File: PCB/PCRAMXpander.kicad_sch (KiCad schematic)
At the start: 24 parts, among them J1 Bus_ISA_16bit, U1 ATF16V8B-15PU, U2 SN74LVCR16245ADGGR, U3 SN74LVC16244ADGGR, U4 SN74LVC16244A, U5 AS6C3216A-55TIN, U6 AS6C3216A-55TIN, U7 SN74LVC573APWR

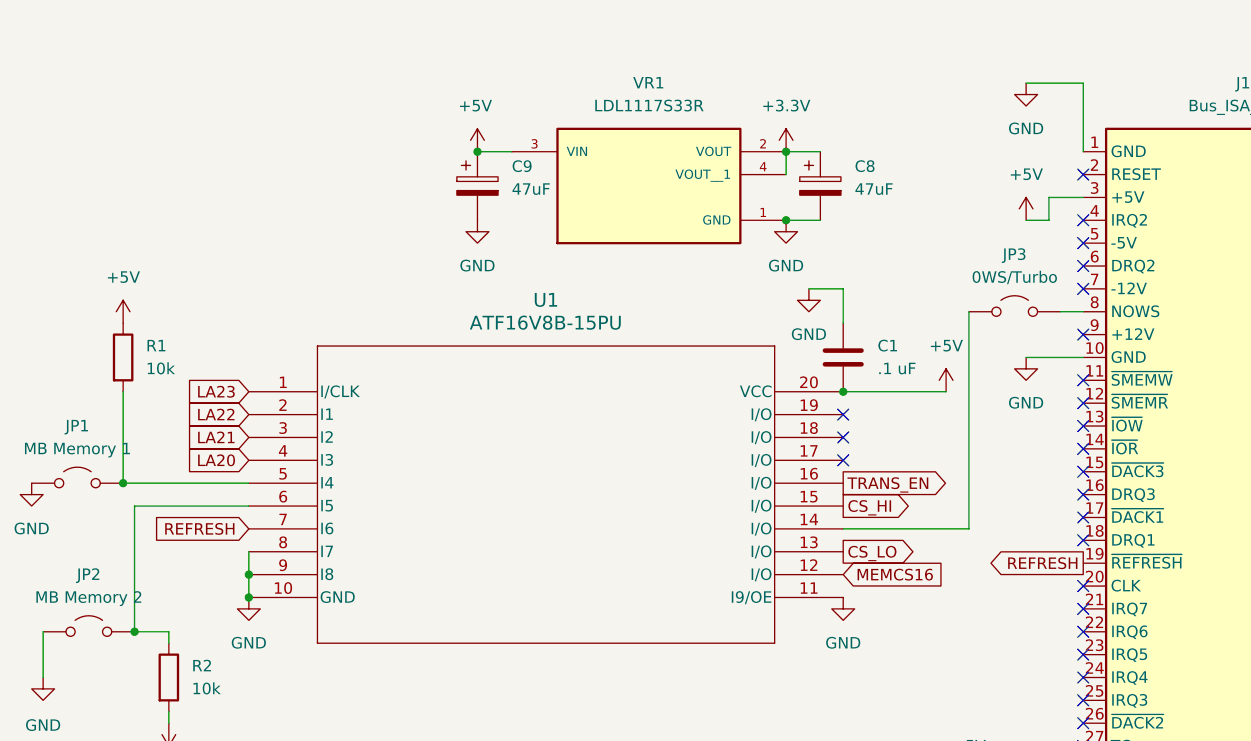
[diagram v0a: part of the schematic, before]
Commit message: Silkscreen updates, reset line wired
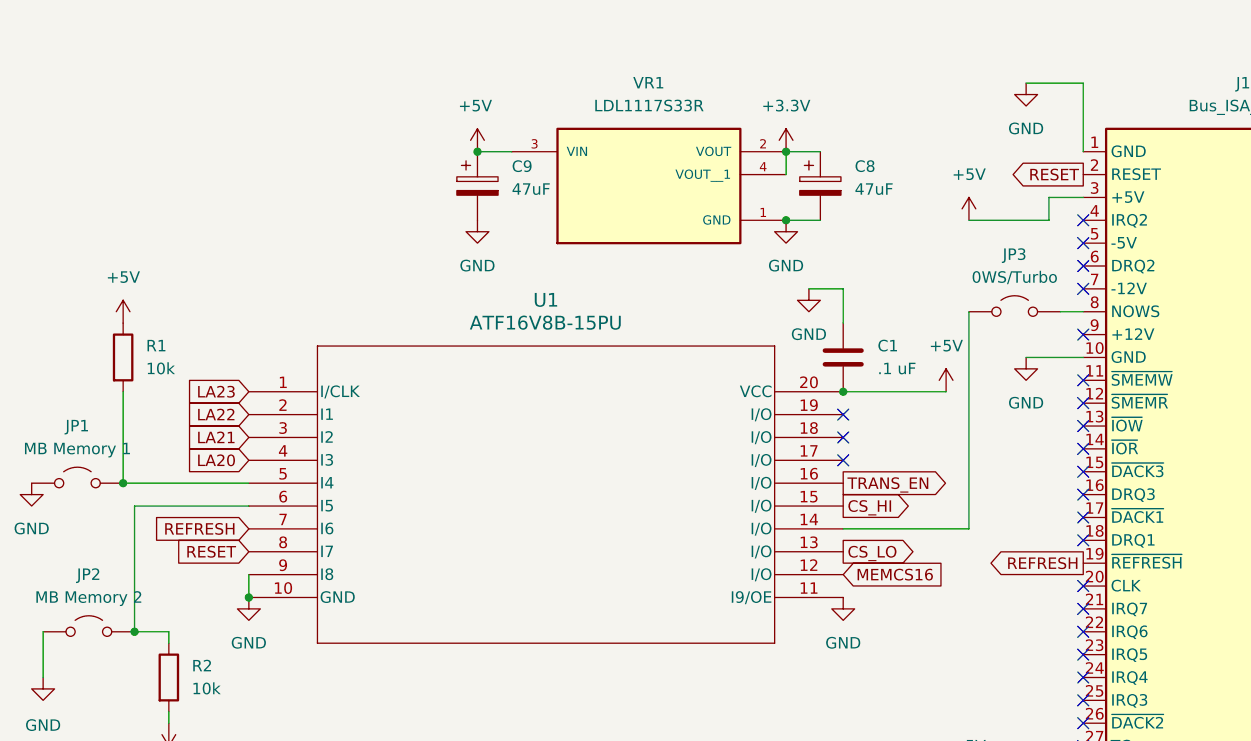
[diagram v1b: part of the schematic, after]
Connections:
- net GND: no longer U1.8 (I7)
- net RESET: now reaches J1.2 (RESET)
- net RESET: now also U1.8 (I7)
- no-connect marks 51 -> 50
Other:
- title: PC RAM Expander 8MB -> PCRAMXpander 8MB
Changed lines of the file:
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@@
 	(paper "B")
 	(title_block
-		(title "PC RAM Expander 8MB")
+		(title "PCRAMXpander 8MB")
 		(date "1/11/2026")
 		(rev "1.0")
@@
 	)
 	(junction
-		(at 41.91 179.07)
-		(diameter 0)
-		(color 0 0 0 0)
-	)
-	(junction
 		(at 278.13 43.18)
 		(diameter 0)
@@
 	)
 	(no_connect
-		(at 134.62 134.62)
-	)
-	(no_connect
 		(at 134.62 142.24)
 	)
@@
 	(wire
 		(pts
-			(xy 128.27 139.7) (xy 130.81 139.7)
+			(xy 121.92 139.7) (xy 130.81 139.7)
 		)
 		(stroke
@@
 	(wire
 		(pts
-			(xy 41.91 176.53) (xy 41.91 179.07)
-		)
-		(stroke
-			(width 0)
-			(type default)
-		)
-	)
-	(wire
-		(pts
 			(xy 195.58 194.31) (xy 212.09 194.31)
 		)
@@
 		)
 	)
+	(global_label "RESET"
+		(shape input)
+		(at 41.91 176.53 180)
+		(fields_autoplaced yes)
+		(effects
+			(font
+				(size 1.27 1.27)
+			)
+			(justify right)
+		)
+		(property "Intersheetrefs" "${INTERSHEET_REFS}"
+			(at 33.1797 176.53 0)
+			(effects
+				(font
+					(size 1.27 1.27)
+				)
+				(justify right)
+				(hide yes)
+			)
+		)
+	)
 	(global_label "D6"
 		(shape bidirectional)
@@
 		)
 	)
+	(global_label "RESET"
+		(shape output)
+		(at 134.62 134.62 180)
+		(fields_autoplaced yes)
+		(effects
+			(font
+				(size 1.27 1.27)
+			)
+			(justify right)
+		)
+		(property "Intersheetrefs" "${INTERSHEET_REFS}"
+			(at 125.8897 134.62 0)
+			(effects
+				(font
+					(size 1.27 1.27)
+				)
+				(justify right)
+				(hide yes)
+			)
+		)
+	)
 	(global_label "BA05"
 		(shape output)
@@
 	(symbol
 		(lib_id "power:+5V")
-		(at 128.27 139.7 0)
+		(at 121.92 139.7 0)
 		(unit 1)
 		(exclude_from_sim no)
@@
 		(fields_autoplaced yes)
 		(property "Reference" "#PWR024"
-			(at 128.27 143.51 0)
+			(at 121.92 143.51 0)
 			(effects
 				(font
@@
 		)
 		(property "Value" "+5V"
-			(at 128.27 134.62 0)
+			(at 121.92 134.62 0)
 			(effects
 				(font
@@
 		)
 		(property "Footprint" ""
-			(at 128.27 139.7 0)
+			(at 121.92 139.7 0)
 			(effects
 				(font
@@
 		)
 		(property "Datasheet" ""
-			(at 128.27 139.7 0)
+			(at 121.92 139.7 0)
 			(effects
 				(font
@@
 		)
 		(property "Description" "Power symbol creates a global label with name \"+5V\""
-			(at 128.27 139.7 0)
+			(at 121.92 139.7 0)
 			(effects
 				(font

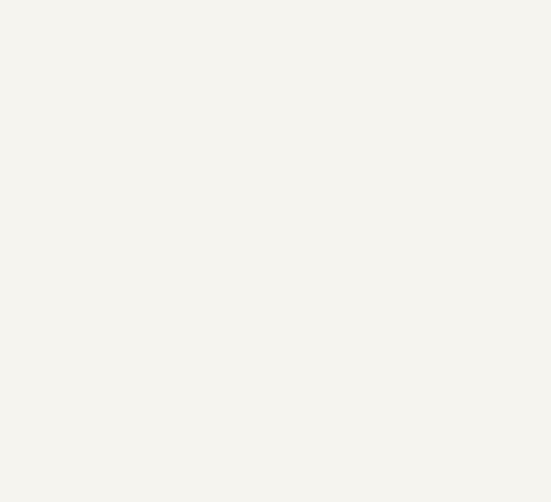
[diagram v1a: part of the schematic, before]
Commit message: Added mounting holes
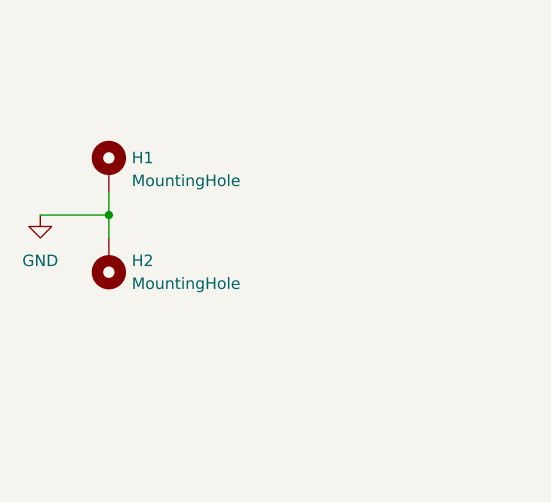
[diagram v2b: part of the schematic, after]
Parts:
- added H1, H2: MountingHole, MountingHole:MountingHole_3.2mm_M3_Pad_Via, symbol Mechanical:MountingHole_Pad
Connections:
- net GND: now also H1.1, H2.1
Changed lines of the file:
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@@
 	)
 	(junction
+		(at 25.4 36.83)
+		(diameter 0)
+		(color 0 0 0 0)
+	)
+	(junction
 		(at 321.31 81.28)
 		(diameter 0)
@@
 	(wire
 		(pts
+			(xy 25.4 34.29) (xy 25.4 36.83)
+		)
+		(stroke
+			(width 0)
+			(type default)
+		)
+	)
+	(wire
+		(pts
 			(xy 144.78 39.37) (xy 162.56 39.37)
 		)
@@
 	(wire
 		(pts
+			(xy 25.4 36.83) (xy 25.4 39.37)
+		)
+		(stroke
+			(width 0)
+			(type default)
+		)
+	)
+	(wire
+		(pts
 			(xy 313.69 199.39) (xy 323.85 199.39)
 		)
@@
 	(wire
 		(pts
+			(xy 17.78 36.83) (xy 25.4 36.83)
+		)
+		(stroke
+			(width 0)
+			(type default)
+		)
+	)
+	(wire
+		(pts
 			(xy 198.12 199.39) (xy 212.09 199.39)
 		)
@@
 	)
 	(symbol
+		(lib_id "Mechanical:MountingHole_Pad")
+		(at 25.4 41.91 180)
+		(unit 1)
+		(exclude_from_sim no)
+		(in_bom no)
+		(on_board yes)
+		(dnp no)
+		(fields_autoplaced yes)
+		(property "Reference" "H2"
+			(at 27.94 41.9099 0)
+			(effects
+				(font
+					(size 1.27 1.27)
+				)
+				(justify right)
+			)
+		)
+		(property "Value" "MountingHole"
+			(at 27.94 44.4499 0)
+			(effects
+				(font
+					(size 1.27 1.27)
+				)
+				(justify right)
+			)
+		)
+		(property "Footprint" "MountingHole:MountingHole_3.2mm_M3_Pad_Via"
+			(at 25.4 41.91 0)
+			(effects
+				(font
+					(size 1.27 1.27)
+				)
+				(hide yes)
+			)
+		)
+		(property "Datasheet" "~"
+			(at 25.4 41.91 0)
+			(effects
+				(font
+					(size 1.27 1.27)
+				)
+				(hide yes)
+			)
+		)
+		(property "Description" "Mounting Hole with connection"
+			(at 25.4 41.91 0)
+			(effects
+				(font
+					(size 1.27 1.27)
+				)
+				(hide yes)
+			)
+		)
+		(pin "1"
+		)
+		(instances
+			(project "PCRAMXpander"
+				(path "/1cf6e2a4-b983-419d-81f7-8fbd15ee10a7"
+					(reference "H2")
+					(unit 1)
+				)
+			)
+		)
+	)
+	(symbol
 		(lib_id "ATF16V8B_15PU_2026-01-01_19-13-25:ATF16V8B-15PU")
 		(at 41.91 158.75 0)
@@
 	)
 	(symbol
+		(lib_id "Mechanical:MountingHole_Pad")
+		(at 25.4 31.75 0)
+		(unit 1)
+		(exclude_from_sim no)
+		(in_bom no)
+		(on_board yes)
+		(dnp no)
+		(property "Reference" "H1"
+			(at 27.94 30.4799 0)
+			(effects
+				(font
+					(size 1.27 1.27)
+				)
+				(justify left)
+			)
+		)
+		(property "Value" "MountingHole"
+			(at 27.94 33.0199 0)
+			(effects
+				(font
+					(size 1.27 1.27)
+				)
+				(justify left)
+			)
+		)
+		(property "Footprint" "MountingHole:MountingHole_3.2mm_M3_Pad_Via"
+			(at 25.4 31.75 0)
+			(effects
+				(font
+					(size 1.27 1.27)
+				)
+				(hide yes)
+			)
+		)
+		(property "Datasheet" "~"
+			(at 25.4 31.75 0)
+			(effects
+				(font
+					(size 1.27 1.27)
+				)
+				(hide yes)
+			)
+		)
+		(property "Description" "Mounting Hole with connection"
+			(at 25.4 31.75 0)
+			(effects
+				(font
+					(size 1.27 1.27)
+				)
+				(hide yes)
+			)
+		)
+		(pin "1"
+		)
+		(instances
+			(project ""
+				(path "/1cf6e2a4-b983-419d-81f7-8fbd15ee10a7"
+					(reference "H1")
+					(unit 1)
+				)
+			)
+		)
+	)
+	(symbol
 		(lib_id "power:GND")
 		(at 101.6 139.7 0)
@@
 					(unit 1)
 				)
+			)
+		)
+	)
+	(symbol
+		(lib_id "power:GND")
+		(at 17.78 36.83 0)
+		(unit 1)
+		(exclude_from_sim no)
+		(in_bom yes)
+		(on_board yes)
+		(dnp no)
+		(property "Reference" "#PWR045"
+			(at 17.78 43.18 0)
+			(effects
+				(font
+					(size 1.27 1.27)
+				)
+				(hide yes)
+			)
+		)
+		(property "Value" "GND"
+			(at 17.78 41.91 0)
+			(effects
+				(font
+					(size 1.27 1.27)
+				)
+			)
+		)
+		(property "Footprint" ""
+			(at 17.78 36.83 0)
+			(effects
+				(font
+					(size 1.27 1.27)
+				)
+				(hide yes)
+			)
+		)
+		(property "Datasheet" ""
+			(at 17.78 36.83 0)
+			(effects
+				(font
+					(size 1.27 1.27)
+				)
+				(hide yes)
+			)
+		)
+		(property "Description" "Power symbol creates a global label with name \"GND\" , ground"
+			(at 17.78 36.83 0)
+			(effects
+				(font
+					(size 1.27 1.27)
+				)
+				(hide yes)
+			)
+		)
+		(pin "1"
+		)
+		(instances
+			(project "PCRAMXpander"
+				(path "/1cf6e2a4-b983-419d-81f7-8fbd15ee10a7"
+					(reference "#PWR045")
+					(unit 1)
+				)

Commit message: Fixing value
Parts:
- U4: value SN74LVC16244A -> SN74LVC541APWR
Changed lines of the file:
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@@
 			)
 		)
-		(property "Value" "SN74LVC16244A"
+		(property "Value" "SN74LVC541APWR"
 			(at 264.16 49.53 0)
 			(effects
